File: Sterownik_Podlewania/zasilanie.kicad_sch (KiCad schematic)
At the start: 12 parts, among them J14 Screw_Terminal_01x02, J15 Barrel_Jack_MountingPin, J16 Screw_Terminal_01x02, SW8 SW_Push_DPDT, U3 L7805, U4 LM1117DT-3.3

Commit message: Poprawki estetyczne schematu
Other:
- moved on the sheet: C4, C5, C6, C7, D13, D14, J14, J15, J16, SW8, U3, U4

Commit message: Dodanie gniazd ethernet, poprawienie większośc ERC
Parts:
- removed U4: LM1117DT-3.3, Package_TO_SOT_SMD:TO-252-3_TabPin2, symbol Regulator_Linear:LM1117DT-3.3
- added U4: LM1085-3.3, symbol Regulator_Linear:LM1085-3.3
- renumbered C7 to C10, C4 to C7, C5 to C8, C6 to C9, D13 to D19, D14 to D20, J14 to J15, J15 to J17, SW8 to SW7
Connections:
- net +5V: now also U4.3 (VI)
- net GND: now also U4.1 (GND)
- net at C10.1, D20.2 (A): now also U4.2 (VO)
- net 3.3V renamed +3.3V
- net GND_Vp renamed GND_VP
- net Vp renamed VP
- no-connect marks 0 -> 1
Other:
- note added: "możlwość wybrania zasilania zaworów zasilanie zewnętrzne/zasilanie urządzenia (12V)"
- note added: "zewnętrzena zasilanie zaworów (przekaźników)"
- title: (none) -> Sterownik podlewania V1.1
- moved on the sheet: SW7

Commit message: Wstępny układ PCB
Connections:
- net L_230V renamed 230VAC

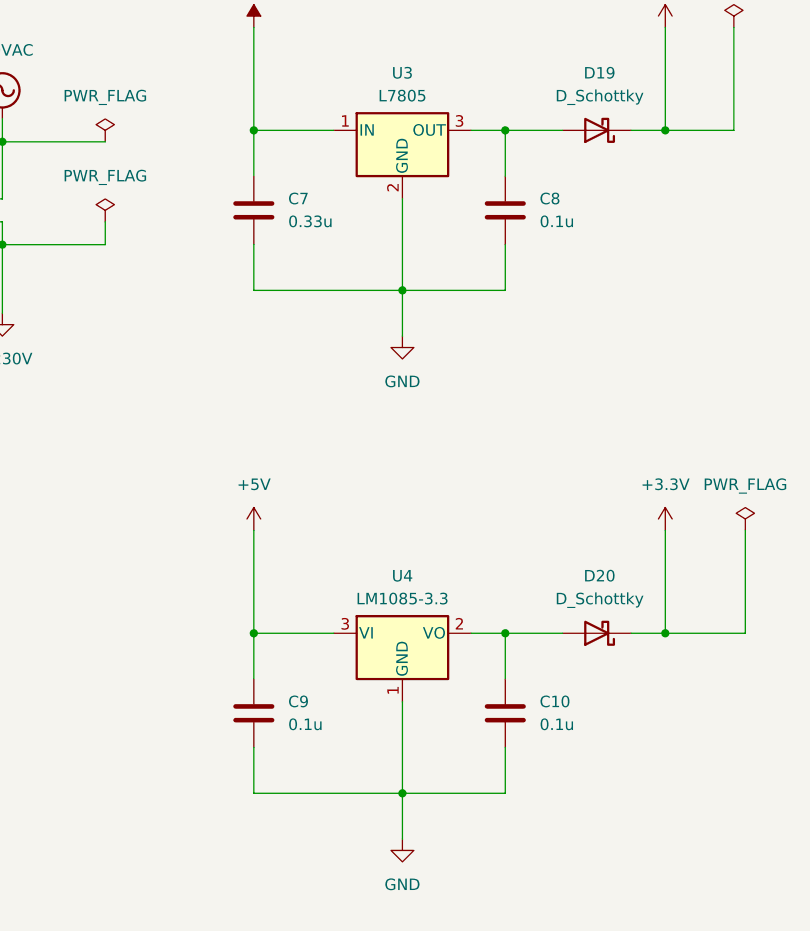
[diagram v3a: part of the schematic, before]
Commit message: Dodanie footprintów schotky, kondesatorów
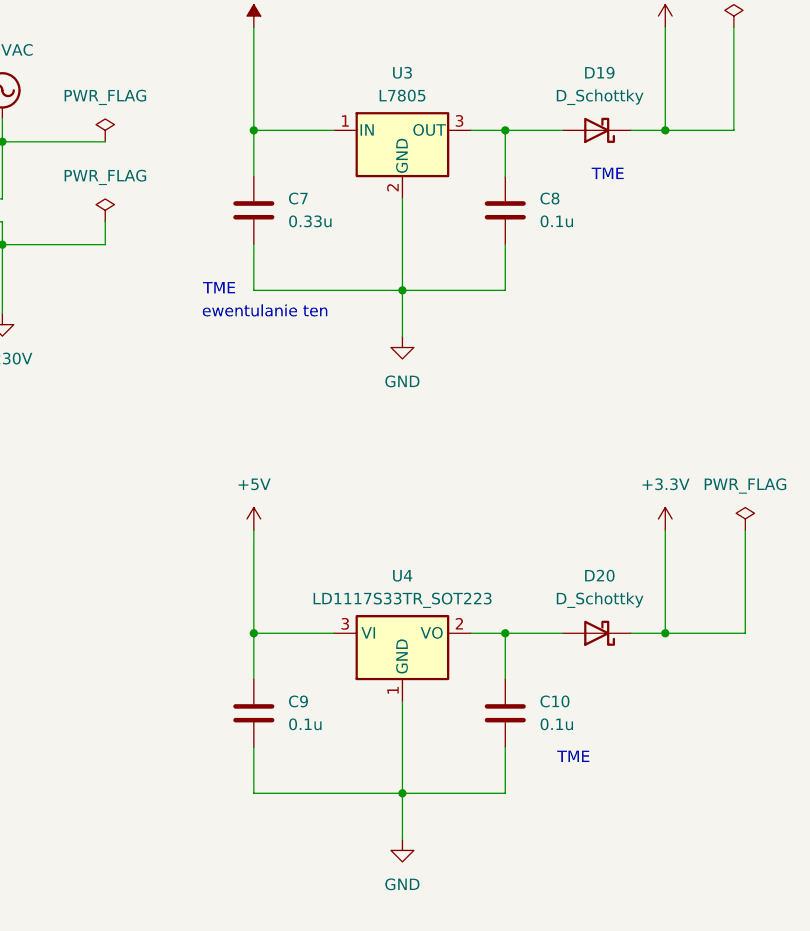
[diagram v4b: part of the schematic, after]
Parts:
- removed U4: LM1085-3.3, symbol Regulator_Linear:LM1085-3.3
- added U4: LD1117S33TR_SOT223, Package_TO_SOT_SMD:SOT-223-3_TabPin2, symbol Regulator_Linear:LD1117S33TR_SOT223
- C10, C8, C9: footprint (none) -> Capacitor_THT:C_Disc_D3.0mm_W1.6mm_P2.50mm
- C7: footprint (none) -> Capacitor_THT:CP_Axial_L10.0mm_D4.5mm_P15.00mm_Horizontal
- D19, D20: footprint (none) -> Diode_SMD:D_SOD-123
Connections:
- net +5V: now also U4.3 (VI)
- net GND: now also U4.1 (GND)
- net at C10.1, D20.2 (A): now also U4.2 (VO)
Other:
- note added: "TME"
- note added: "ewentulanie ten"
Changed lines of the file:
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@@
 		(comment 2 "Filip Gajewski")
+	)
+	(text "ewentulanie ten"
+		(exclude_from_sim no)
+		(at 156.21 73.66 0)
+		(effects
+			(font
+				(size 1.27 1.27)
+			)
+			(href "https://www.tme.eu/pl/details/vs1hr33mb054000ce0/kondensatory-elektrolityczne-smd/changzhou-huawei-electronic/")
+		)
+	)
+	(text "TME"
+		(exclude_from_sim no)
+		(at 190.5 123.19 0)
+		(effects
+			(font
+				(size 1.27 1.27)
+			)
+			(href "https://www.tme.eu/pl/details/cc-100n/kondensatory-ceramiczne/sr-passives/")
+		)
+	)
+	(text "TME"
+		(exclude_from_sim no)
+		(at 194.31 58.42 0)
+		(effects
+			(font
+				(size 1.27 1.27)
+			)
+			(href "https://www.tme.eu/pl/details/bat46w-dio/diody-schottky-smd/diotec-semiconductor/bat46w/")
+		)
+	)
+	(text "TME"
+		(exclude_from_sim no)
+		(at 151.13 71.12 0)
+		(effects
+			(font
+				(size 1.27 1.27)
+			)
+			(href "https://www.tme.eu/pl/details/jfw-330n_310-p15/kondensatory-foliowe-tht/jb-capacitors/")
+		)
 	)
 	(text "możlwość wybrania zasilania zaworów \nzasilanie zewnętrzne/zasilanie urządzenia (12V)"
@@
 			)
 		)
-		(property "Footprint" ""
+		(property "Footprint" "Capacitor_THT:CP_Axial_L10.0mm_D4.5mm_P15.00mm_Horizontal"
 			(at 155.9052 66.04 0)
 			(effects
@@
 			)
 		)
-		(property "Footprint" ""
+		(property "Footprint" "Capacitor_THT:C_Disc_D3.0mm_W1.6mm_P2.50mm"
 			(at 183.8452 121.92 0)
 			(effects
@@
 	)
 	(symbol
+		(lib_id "Regulator_Linear:LD1117S33TR_SOT223")
+		(at 171.45 109.22 0)
+		(unit 1)
+		(exclude_from_sim no)
+		(in_bom yes)
+		(on_board yes)
+		(dnp no)
+		(fields_autoplaced yes)
+		(property "Reference" "U4"
+			(at 171.45 102.87 0)
+			(effects
+				(font
+					(size 1.27 1.27)
+				)
+			)
+		)
+		(property "Value" "LD1117S33TR_SOT223"
+			(at 171.45 105.41 0)
+			(effects
+				(font
+					(size 1.27 1.27)
+				)
+			)
+		)
+		(property "Footprint" "Package_TO_SOT_SMD:SOT-223-3_TabPin2"
+			(at 171.45 104.14 0)
+			(effects
+				(font
+					(size 1.27 1.27)
+				)
+				(hide yes)
+			)
+		)
+		(property "Datasheet" "http://www.st.com/st-web-ui/static/active/en/resource/technical/document/datasheet/CD00000544.pdf"
+			(at 173.99 115.57 0)
+			(effects
+				(font
+					(size 1.27 1.27)
+				)
+				(hide yes)
+			)
+		)
+		(property "Description" "800mA Fixed Low Drop Positive Voltage Regulator, Fixed Output 3.3V, SOT-223"
+			(at 171.45 109.22 0)
+			(effects
+				(font
+					(size 1.27 1.27)
+				)
+				(hide yes)
+			)
+		)
+		(pin "1"
+		)
+		(pin "2"
+		)
+		(pin "3"
+		)
+		(instances
+			(project ""
+				(path "/a66bdf1f-0e2a-4cc5-beb1-605f2a3b9885/73dd885a-a6d0-4e55-a40e-d99ff27ab8ee"
+					(reference "U4")
+					(unit 1)
+				)
+			)
+		)
+	)
+	(symbol
 		(lib_id "power:GND")
 		(at 127 73.66 0)
@@
 			)
 		)
-		(property "Footprint" ""
+		(property "Footprint" "Capacitor_THT:C_Disc_D3.0mm_W1.6mm_P2.50mm"
 			(at 183.8452 66.04 0)
 			(effects
@@
 	)
 	(symbol
-		(lib_id "Regulator_Linear:LM1085-3.3")
-		(at 171.45 109.22 0)
-		(unit 1)
-		(exclude_from_sim no)
-		(in_bom yes)
-		(on_board yes)
-		(dnp no)
-		(fields_autoplaced yes)
-		(property "Reference" "U4"
-			(at 171.45 102.87 0)
-			(effects
-				(font
-					(size 1.27 1.27)
-				)
-			)
-		)
-		(property "Value" "LM1085-3.3"
-			(at 171.45 105.41 0)
-			(effects
-				(font
-					(size 1.27 1.27)
-				)
-			)
-		)
-		(property "Footprint" ""
-			(at 171.45 102.87 0)
-			(effects
-				(font
-					(size 1.27 1.27)
-					(italic yes)
-				)
-				(hide yes)
-			)
-		)
-		(property "Datasheet" "http://www.ti.com/lit/ds/symlink/lm1085.pdf"
-			(at 171.45 109.22 0)
-			(effects
-				(font
-					(size 1.27 1.27)
-				)
-				(hide yes)
-			)
-		)
-		(property "Description" "3A 27V Linear Regulator, Fixed Output 3.3V, TO-220/TO-263"
-			(at 171.45 109.22 0)
-			(effects
-				(font
-					(size 1.27 1.27)
-				)
-				(hide yes)
-			)
-		)
-		(pin "1"
-		)
-		(pin "3"
-		)
-		(pin "2"
-		)
-		(instances
-			(project ""
-				(path "/a66bdf1f-0e2a-4cc5-beb1-605f2a3b9885/73dd885a-a6d0-4e55-a40e-d99ff27ab8ee"
-					(reference "U4")
-					(unit 1)
-				)
-			)
-		)
-	)
-	(symbol
 		(lib_id "power:VPP")
 		(at 96.52 129.54 0)
@@
 			)
 		)
-		(property "Footprint" ""
+		(property "Footprint" "Diode_SMD:D_SOD-123"
 			(at 193.04 109.22 0)
 			(effects
@@
 			)
 		)
-		(property "Footprint" ""
+		(property "Footprint" "Capacitor_THT:C_Disc_D3.0mm_W1.6mm_P2.50mm"
 			(at 155.9052 121.92 0)
 			(effects
@@
 			)
 		)
-		(property "Footprint" ""
+		(property "Footprint" "Diode_SMD:D_SOD-123"
 			(at 193.04 53.34 0)
 			(effects

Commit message: Dodanie modeli 3d, nowy footprint do przełącznika, przerzucenie na drugą stronę płytki elementów, wstępne rozdzielenie elemntów pasywnych
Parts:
- U4: footprint Package_TO_SOT_SMD:SOT-223-3_TabPin2 -> Package_TO_SOT_THT:TO-220-3_Vertical
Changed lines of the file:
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@@
 			)
 		)
-		(property "Footprint" "Package_TO_SOT_SMD:SOT-223-3_TabPin2"
+		(property "Footprint" "Package_TO_SOT_THT:TO-220-3_Vertical"
 			(at 171.45 104.14 0)
 			(effects

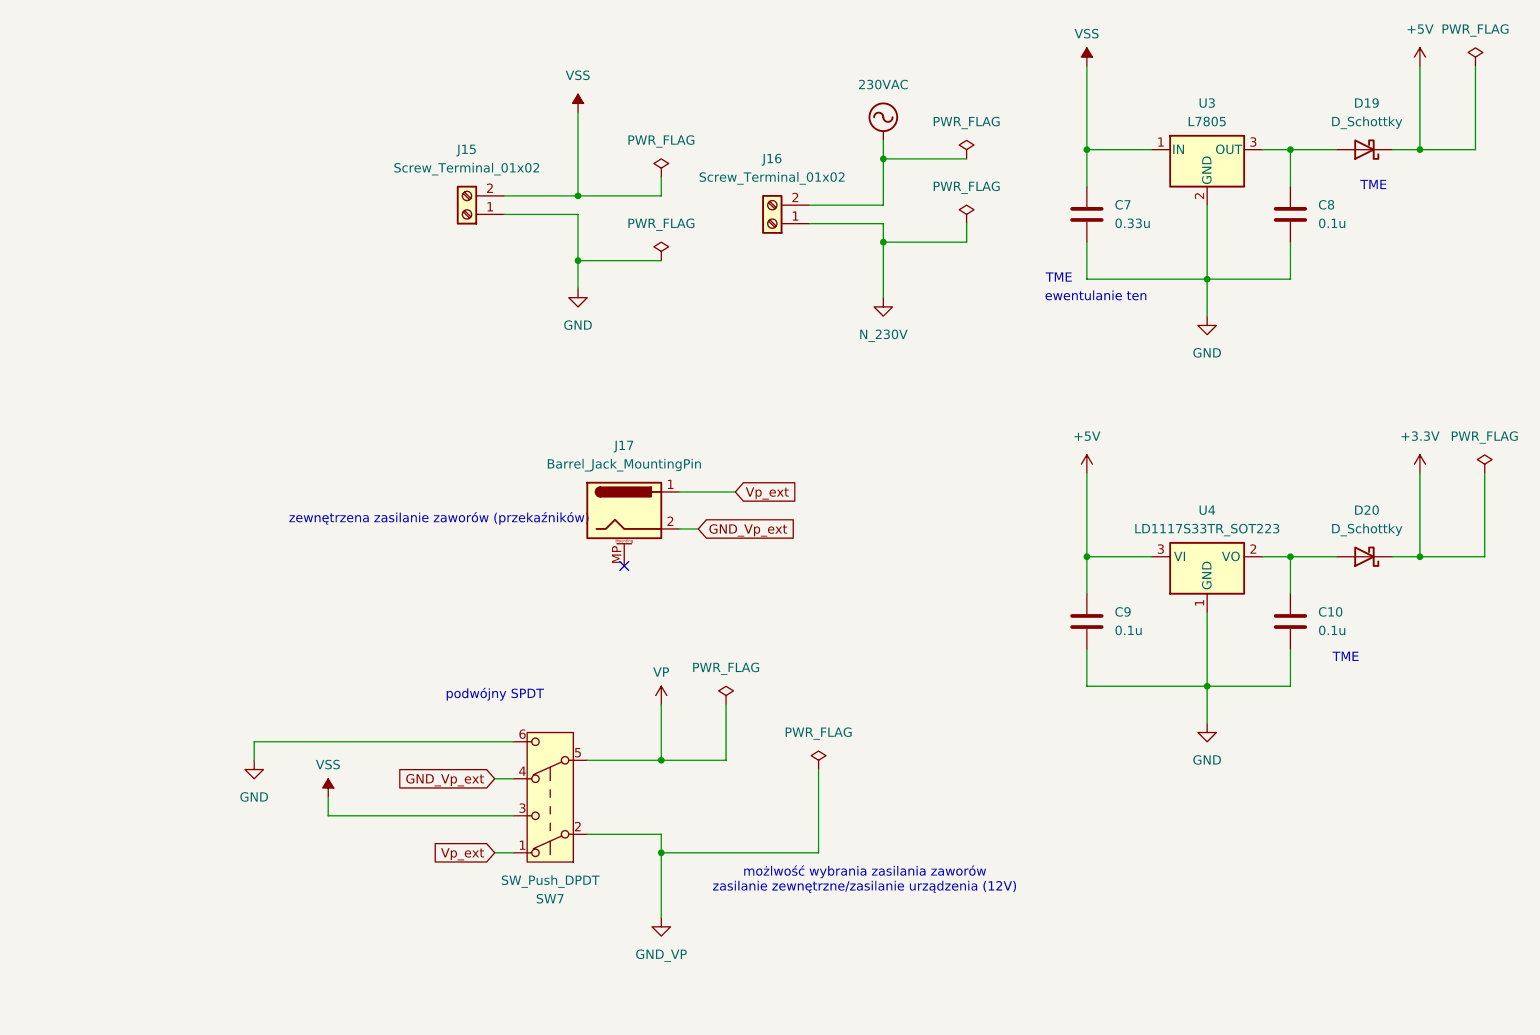
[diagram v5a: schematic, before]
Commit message: dodanie modeli 3d, poprawa footprintu RTC
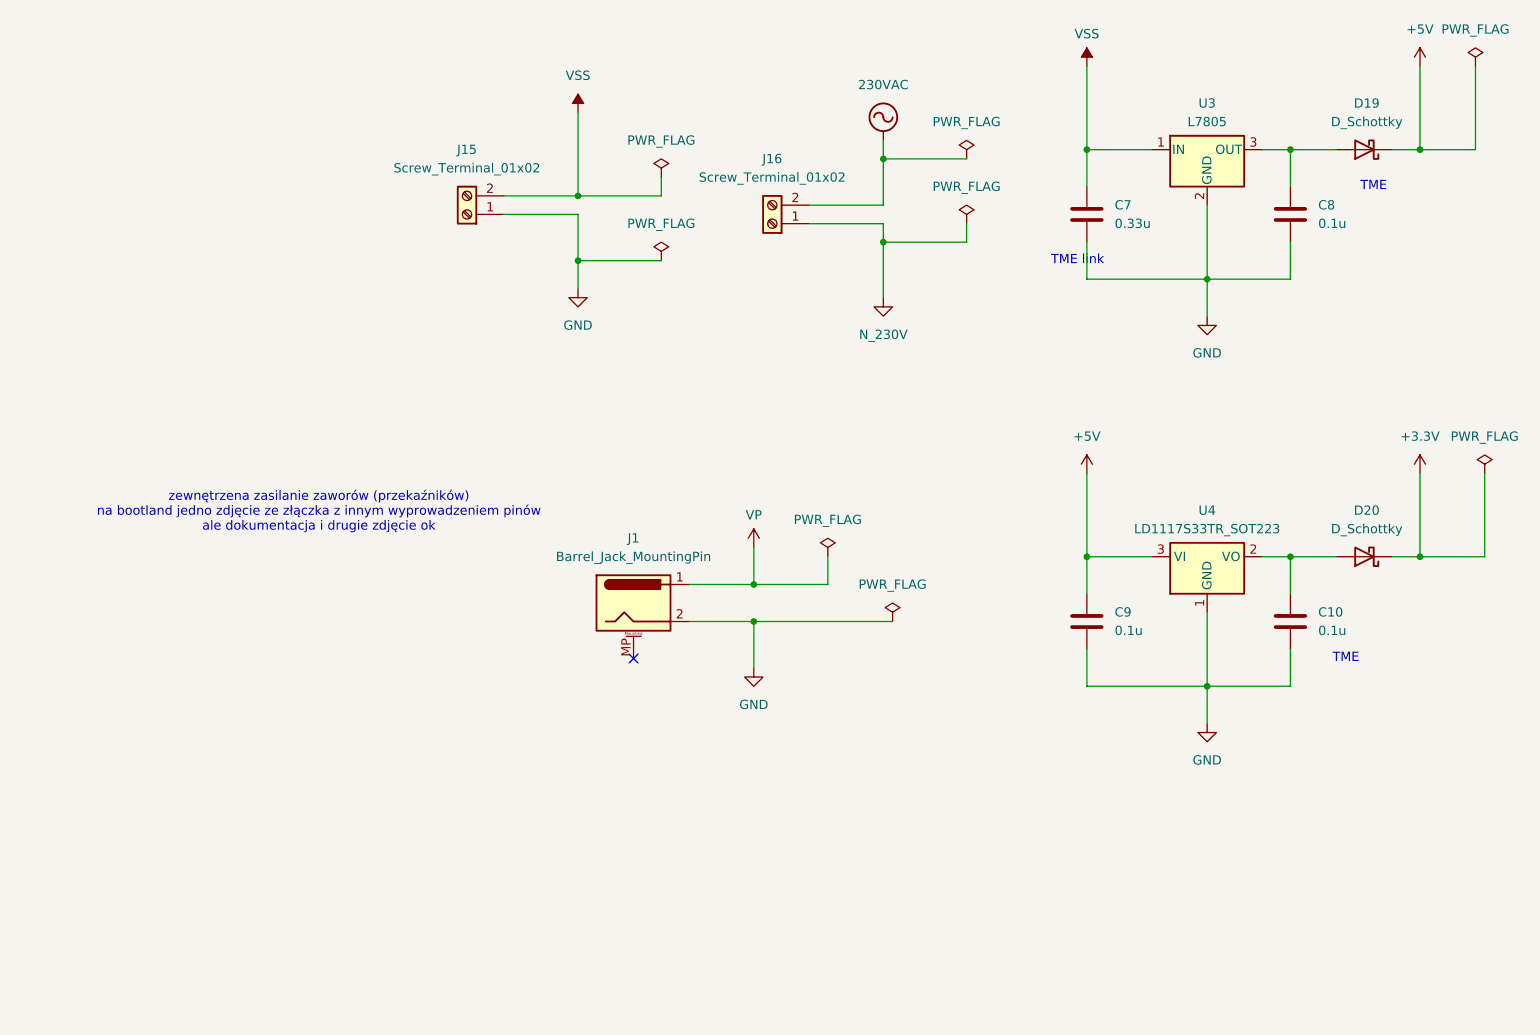
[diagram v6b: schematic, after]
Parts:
- removed J17: Barrel_Jack_MountingPin, symbol Connector:Barrel_Jack_MountingPin
- removed SW7: SW_Push_DPDT, symbol Switch:SW_Push_DPDT
- added J1: Barrel_Jack_MountingPin, Connector_BarrelJack:BarrelJack_GCT_DCJ200-10-A_Horizontal, symbol Connector:Barrel_Jack_MountingPin
- C7: footprint Capacitor_THT:CP_Axial_L10.0mm_D4.5mm_P15.00mm_Horizontal -> Capacitor_SMD:CP_Elec_4x5.4
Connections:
- net GND: now also J1.2
- net VP: now also J1.1
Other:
- note added: "TME link"
- note added: "zewnętrzena zasilanie zaworów (przekaźników) na bootland jedno zdjęcie ze złączka z innym wyprowadzeniem pinów ale dokumentacja i drugie zdjęcie ok"
- note removed: "ewentulanie ten"
- note removed: "możlwość wybrania zasilania zaworów zasilanie zewnętrzne/zasilanie urządzenia (12V)"
- note removed: "podwójny SPDT"
- note removed: "zewnętrzena zasilanie zaworów (przekaźników)"

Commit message: Wstępny finalny rozkład płytki, narysowanie outlinu
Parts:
- U4: footprint Package_TO_SOT_THT:TO-220-3_Vertical -> Package_TO_SOT_SMD:SOT-223
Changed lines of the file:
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@@
 			)
 		)
-		(property "Footprint" "Package_TO_SOT_THT:TO-220-3_Vertical"
+		(property "Footprint" "Package_TO_SOT_SMD:SOT-223"
 			(at 171.45 104.14 0)
 			(effects

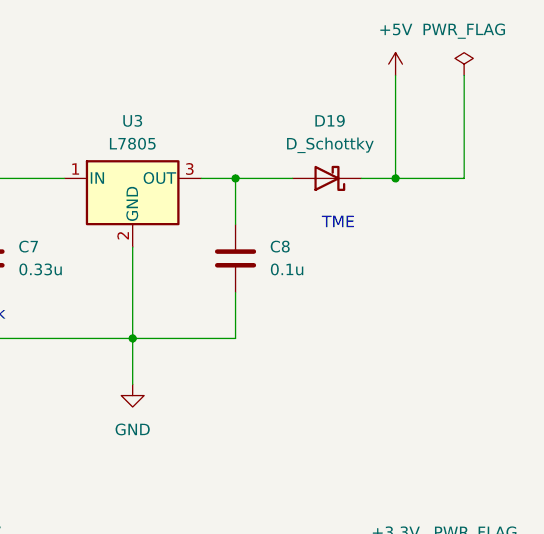
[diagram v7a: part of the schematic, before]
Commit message: Zmiana footprintó diód przekaźnika na schottky,finalne ułożenie  przekaźników, diód itp
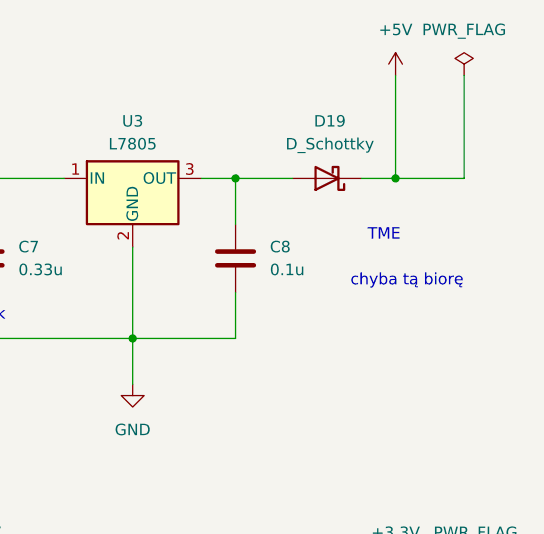
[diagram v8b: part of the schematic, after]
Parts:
- D19, D20: footprint Diode_SMD:D_SOD-123 -> Diode_SMD:D_1206_3216Metric
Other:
- note added: "chyba tą biorę"
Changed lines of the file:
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@@
 	(text "TME"
 		(exclude_from_sim no)
-		(at 194.31 58.42 0)
+		(at 199.39 59.69 0)
 		(effects
 			(font
@@
 			)
 			(href "https://www.tme.eu/pl/details/bat46w-dio/diody-schottky-smd/diotec-semiconductor/bat46w/")
+		)
+	)
+	(text "chyba tą biorę\n"
+		(exclude_from_sim no)
+		(at 201.93 64.77 0)
+		(effects
+			(font
+				(size 1.27 1.27)
+			)
+			(href "https://www.tme.eu/pl/details/sd1206s100s1r0/diody-schottky-smd/kyocera-avx/")
 		)
 	)
@@
 			)
 		)
-		(property "Footprint" "Diode_SMD:D_SOD-123"
+		(property "Footprint" "Diode_SMD:D_1206_3216Metric"
 			(at 193.04 109.22 0)
 			(effects
@@
 			)
 		)
-		(property "Footprint" "Diode_SMD:D_SOD-123"
+		(property "Footprint" "Diode_SMD:D_1206_3216Metric"
 			(at 193.04 53.34 0)
 			(effects
